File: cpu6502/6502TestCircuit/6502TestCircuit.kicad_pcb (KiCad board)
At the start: 4 copper layers, 45.7 x 40.6 mm, 15 parts, among them J1 Power, J2 Power, J5 Ext RST, SW1 Reset, U6 L7805, U9 DS1813

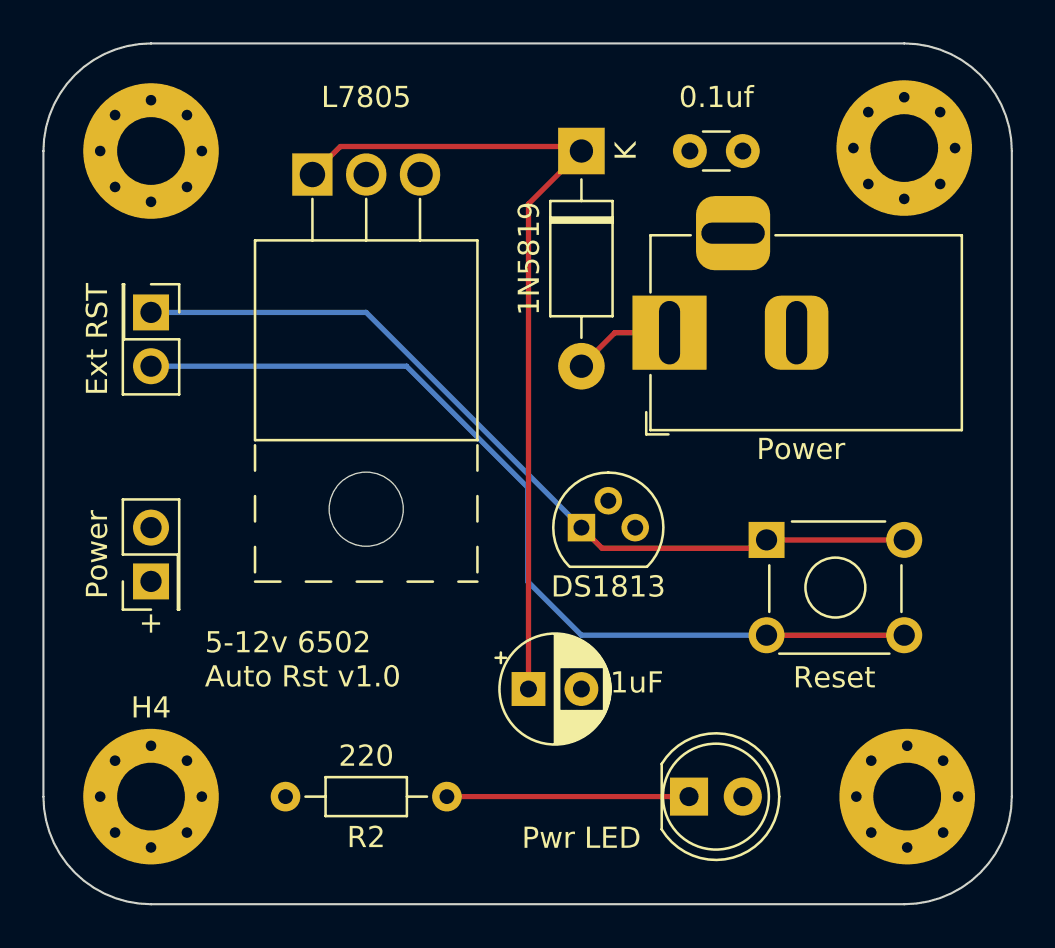
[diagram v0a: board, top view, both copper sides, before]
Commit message: Sent test circuit to PCBWay
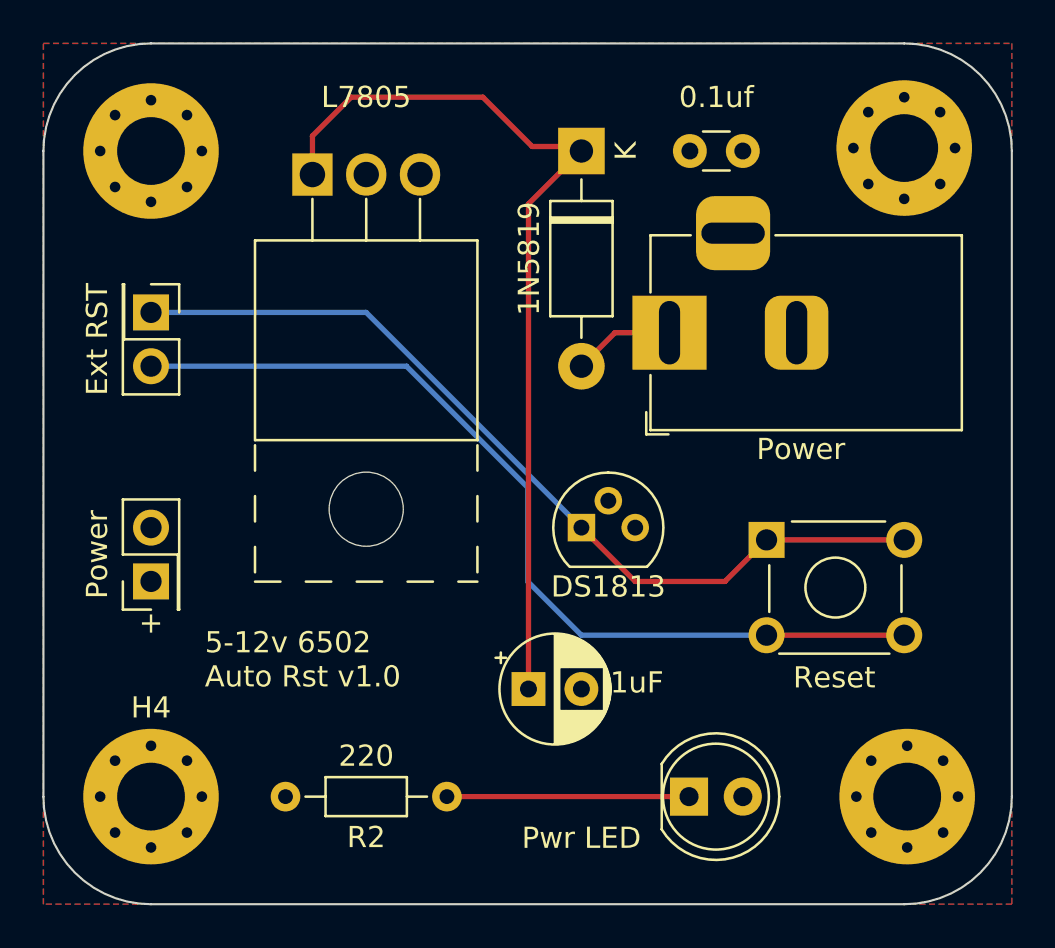
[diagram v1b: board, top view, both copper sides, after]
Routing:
- net Net-(D3-K): track 39.8 -> 42.8 mm
- net Net-(J5-Pin_1): track 40.3 -> 41.6 mm
- added copper zone on B.Cu, net +5V
- added copper zone on F.Cu, net GND
- removed copper zone on In2.Cu, net +5V
- removed copper zone on In1.Cu, net GND
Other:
- copper layers 4 -> 2
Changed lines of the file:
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@@
   (layers
     (0 "F.Cu" signal)
-    (1 "In1.Cu" power "GND")
-    (2 "In2.Cu" power "PWR")
     (31 "B.Cu" signal)
     (32 "B.Adhes" user "B.Adhesive")
@@
       (layer "F.Mask" (type "Top Solder Mask") (thickness 0.01))
       (layer "F.Cu" (type "copper") (thickness 0.035))
-      (layer "dielectric 1" (type "prepreg") (thickness 0.1) (material "FR4") (epsilon_r 4.5) (loss_tangent 0.02))
-      (layer "In1.Cu" (type "copper") (thickness 0.035))
-      (layer "dielectric 2" (type "core") (thickness 1.24) (material "FR4") (epsilon_r 4.5) (loss_tangent 0.02))
-      (layer "In2.Cu" (type "copper") (thickness 0.035))
-      (layer "dielectric 3" (type "prepreg") (thickness 0.1) (material "FR4") (epsilon_r 4.5) (loss_tangent 0.02))
+      (layer "dielectric 1" (type "core") (thickness 1.51) (material "FR4") (epsilon_r 4.5) (loss_tangent 0.02))
       (layer "B.Cu" (type "copper") (thickness 0.035))
       (layer "B.Mask" (type "Bottom Solder Mask") (thickness 0.01))
@@
     (effects (font (size 1 1) (thickness 0.15)) (justify bottom))
   )
-  (segment (start 142.025 73.445) (end 130.865 73.445) (width 0.25) (layer "F.Cu") (net 1))
+  (segment (start 137.59 71.12) (end 131.365 71.12) (width 0.25) (layer "F.Cu") (net 1))
+  (segment (start 129.54 72.945) (end 129.54 74.77) (width 0.25) (layer "F.Cu") (net 1))
+  (segment (start 131.365 71.12) (end 129.54 72.945) (width 0.25) (layer "F.Cu") (net 1))
   (segment (start 139.74 76.16) (end 142.24 73.66) (width 0.25) (layer "F.Cu") (net 1))
-  (segment (start 130.865 73.445) (end 129.54 74.77) (width 0.25) (layer "F.Cu") (net 1))
+  (segment (start 142.025 73.445) (end 139.915 73.445) (width 0.25) (layer "F.Cu") (net 1))
+  (segment (start 139.915 73.445) (end 137.59 71.12) (width 0.25) (layer "F.Cu") (net 1))
+  (segment (start 139.74 99.06) (end 139.74 76.16) (width 0.25) (layer "F.Cu") (net 1))
   (segment (start 142.24 73.66) (end 142.025 73.445) (width 0.25) (layer "F.Cu") (net 1))
-  (segment (start 139.74 99.06) (end 139.74 76.16) (width 0.25) (layer "F.Cu") (net 1))
   (segment (start 135.89 104.14) (end 147.32 104.14) (width 0.25) (layer "F.Cu") (net 4))
   (segment (start 143.8225 82.2375) (end 142.24 83.82) (width 0.25) (layer "F.Cu") (net 5))
   (segment (start 146.4 82.2375) (end 143.8225 82.2375) (width 0.25) (layer "F.Cu") (net 5))
-  (segment (start 143.215 92.415) (end 142.24 91.44) (width 0.25) (layer "F.Cu") (net 6))
+  (segment (start 149.02 93.98) (end 144.78 93.98) (width 0.25) (layer "F.Cu") (net 6))
   (segment (start 157.48 92.02) (end 150.98 92.02) (width 0.25) (layer "F.Cu") (net 6))
-  (segment (start 150.98 92.02) (end 150.585 92.415) (width 0.25) (layer "F.Cu") (net 6))
-  (segment (start 150.585 92.415) (end 143.215 92.415) (width 0.25) (layer "F.Cu") (net 6))
+  (segment (start 150.98 92.02) (end 149.02 93.98) (width 0.25) (layer "F.Cu") (net 6))
+  (segment (start 144.78 93.98) (end 142.24 91.44) (width 0.25) (layer "F.Cu") (net 6))
   (segment (start 121.92 81.28) (end 132.08 81.28) (width 0.25) (layer "B.Cu") (net 6))
   (segment (start 132.08 81.28) (end 142.24 91.44) (width 0.25) (layer "B.Cu") (net 6))
@@
   (segment (start 139.7 93.98) (end 142.24 96.52) (width 0.25) (layer "B.Cu") (net 7))
   (segment (start 142.24 96.52) (end 150.98 96.52) (width 0.25) (layer "B.Cu") (net 7))
-  (zone (net 2) (net_name "GND") (layer "In1.Cu") (hatch edge 0.5)
+  (zone (net 2) (net_name "GND") (layer "F.Cu") (hatch edge 0.5)
     (connect_pads (clearance 0.5))
     (min_thickness 0.25) (filled_areas_thickness no)
@@
     )
   )
-  (zone (net 3) (net_name "+5V") (layer "In2.Cu") (hatch edge 0.5)
+  (zone (net 3) (net_name "+5V") (layer "B.Cu") (hatch edge 0.5)
     (priority 1)
     (connect_pads (clearance 0.5))

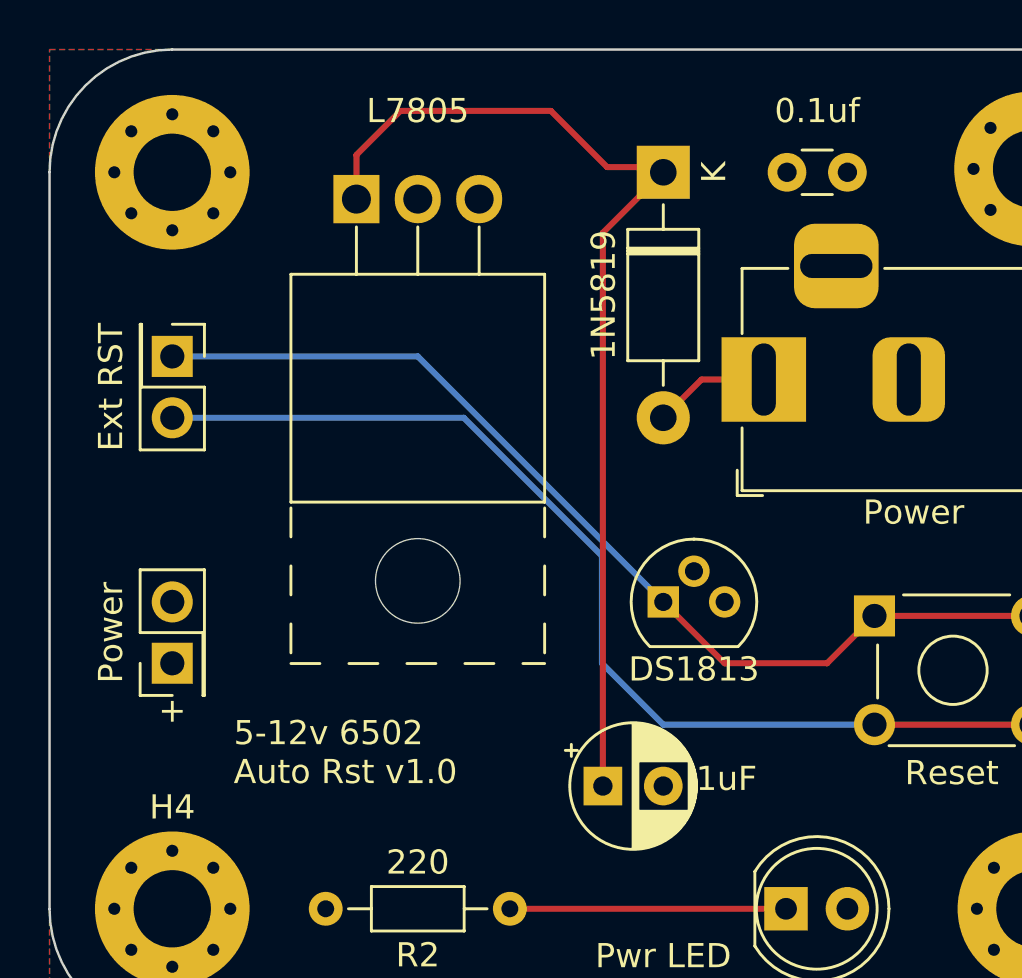
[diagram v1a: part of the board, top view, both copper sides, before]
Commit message: PCB: Add RS232 RCV LED, get pours connected, CODE: checkpoint
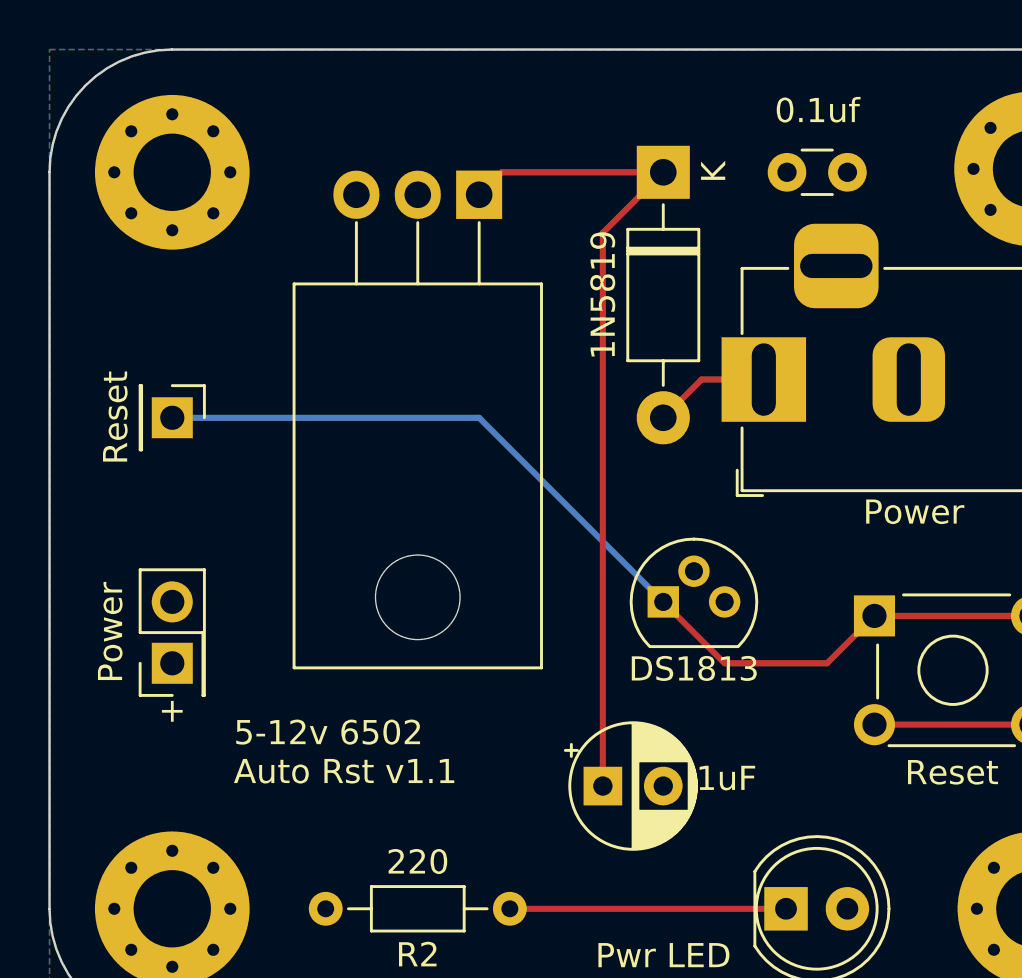
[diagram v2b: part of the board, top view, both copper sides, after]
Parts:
- removed J5: Ext RST, Connector_PinHeader_2.54mm:PinHeader_2x01_P2.54mm_Vertical
- added J3: Reset, Connector_PinHeader_2.54mm:PinHeader_1x01_P2.54mm_Vertical, F.Cu at (121.9, 83.8)
- C7: value 1uF -> 1uF
- U6: footprint Package_TO_SOT_THT:TO-220F-3_Horizontal_TabUp -> Package_TO_SOT_THT:TO-220-3_Horizontal_TabDown
- moved U6 5.08 mm to (134.6, 74.6), turned to 180 degrees
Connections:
- SW1 pad 1: Net-(J5-Pin_1) -> /RST
- SW1 pad 2: /RST -> GND
- U9 pad 1: Net-(J5-Pin_1) -> /RST
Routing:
- net Net-(J5-Pin_1): track 41.6 -> 0.00 mm
- net Net-(D3-K): track 42.8 -> 34.4 mm
- net GND: track 0.00 -> 6.50 mm
- net /RST: track 43.4 -> 40.6 mm
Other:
- board text added: "5-12v 6502 Auto Rst v1.1"
- board text removed: "5-12v 6502 Auto Rst v1.0"

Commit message: code changes (wip), set test PCB 2.0 to PCBway
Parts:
- removed C8: 0.1uf, Capacitor_THT:C_Disc_D3.0mm_W1.6mm_P2.50mm
- removed SW1: Reset, Button_Switch_THT:SW_TH_Tactile_Omron_B3F-10xx
- removed U6: L7805, Package_TO_SOT_THT:TO-220-3_Horizontal_TabDown
- added C1: 1uF, Capacitor_THT:CP_Radial_D5.0mm_P2.50mm, F.Cu at (106.7, 53.3)
- added C2: 0.1uf, Capacitor_THT:C_Disc_D3.0mm_W1.6mm_P2.50mm, F.Cu at (114.3, 71.1)
- added C3: 20pf, Capacitor_THT:C_Disc_D3.0mm_W1.6mm_P2.50mm, F.Cu at (100.3, 61.0)
- added C4: 1uf, Capacitor_THT:C_Disc_D3.0mm_W1.6mm_P2.50mm, F.Cu at (86.4, 38.1)
- added C5: 1uf, Capacitor_THT:C_Disc_D3.0mm_W1.6mm_P2.50mm, F.Cu at (100.3, 45.7)
- added C6: 1uf, Capacitor_THT:C_Disc_D3.0mm_W1.6mm_P2.50mm, F.Cu at (100.3, 48.3)
- added D2: Power LED, LED_THT:LED_D5.0mm, F.Cu at (110.5, 88.9)
- added D4: Rec, LED_THT:LED_D3.0mm, F.Cu at (114.3, 35.6)
- added J4: Power, Connector_BarrelJack:BarrelJack_Horizontal, F.Cu at (109.6, 63.2)
- added J5: RS232, TerminalBlock_TE-Connectivity:TerminalBlock_TE_282834-3_1x03_P2.54mm_Horizontal, F.Cu at (119.4, 43.2)
- added R3: 220, Resistor_THT:R_Axial_DIN0204_L3.6mm_D1.6mm_P7.62mm_Horizontal, F.Cu at (102.9, 86.4)
- added R4: 1M, Resistor_THT:R_Axial_DIN0204_L3.6mm_D1.6mm_P7.62mm_Horizontal, F.Cu at (92.7, 66.0)
- added R5: 220, Resistor_THT:R_Axial_DIN0207_L6.3mm_D2.5mm_P2.54mm_Vertical, F.Cu at (109.2, 36.8)
- added RV2: Contrast (10K), Potentiometer_THT:Potentiometer_Bourns_3386P_Vertical, F.Cu at (71.1, 81.3)
- added SW2: Debug, Button_Switch_THT:SW_TH_Tactile_Omron_B3F-10xx, F.Cu at (97.1, 27.0)
- added SW3: Reset, Button_Switch_THT:SW_TH_Tactile_Omron_B3F-10xx, F.Cu at (65.9, 88.2)
- added SW4: IRQ, Button_Switch_THT:SW_DIP_SPSTx03_Slide_6.7x9.18mm_W7.62mm_P2.54mm_LowProfile, F.Cu at (90.2, 94.0)
- added U1: 6522 (VIA), Package_DIP:DIP-40_W15.24mm_Socket, F.Cu at (43.2, 36.8)
- added U4: L7805, Package_TO_SOT_THT:TO-220-3_Horizontal_TabDown, F.Cu at (119.7, 81.3)
- added U5: DS1813, Package_TO_SOT_THT:TO-92, F.Cu at (96.5, 78.7)
- added U8: MAX232, Package_DIP:DIP-16_W7.62mm_Socket, F.Cu at (86.4, 43.2)
- added Y1: 1.8432 Mhz, Crystal:Crystal_HC49-4H_Vertical, F.Cu at (81.3, 81.3)
- C7: value 1uF -> 1uf; footprint Capacitor_THT:CP_Radial_D5.0mm_P2.50mm -> Capacitor_THT:C_Disc_D3.0mm_W1.6mm_P2.50mm
- D1: value Pwr LED -> 1N5819; footprint LED_THT:LED_D5.0mm -> Diode_THT:D_DO-41_SOD81_P10.16mm_Horizontal
- D3: value 1N5819 -> SB140
- J1: value Power -> CPU; footprint Connector_BarrelJack:BarrelJack_Horizontal -> Connector_PinHeader_2.54mm:PinHeader_1x19_P2.54mm_Vertical
- J2: value Power -> IRQ; footprint Connector_PinHeader_2.54mm:PinHeader_2x01_P2.54mm_Vertical -> Connector_PinHeader_2.54mm:PinHeader_1x01_P2.54mm_Vertical
- J3: value Reset -> LCD; footprint Connector_PinHeader_2.54mm:PinHeader_1x01_P2.54mm_Vertical -> Connector_PinHeader_2.54mm:PinHeader_1x16_P2.54mm_Vertical
- R2: value 220 -> 1K; footprint Resistor_THT:R_Axial_DIN0204_L3.6mm_D1.6mm_P7.62mm_Horizontal -> Resistor_THT:R_Axial_DIN0204_L3.6mm_D1.6mm_P2.54mm_Vertical
- U9: value DS1813 -> 6551 (ACIA); footprint Package_TO_SOT_THT:TO-92 -> Package_DIP:DIP-28_W15.24mm_Socket
- moved H3 145.0 mm to (34.3, 27.9)
- moved H2 124.5 mm to (34.3, 91.4)
- moved J1 117.8 mm to (41.9, 27.9), turned to 90 degrees
- moved J3 100.0 mm to (34.3, 35.6), turned to 0 degrees
- moved R2 78.3 mm to (109.2, 30.5), turned to 90 degrees
- moved H4 76.2 mm to (119.5, 27.9)
- moved U9 64.7 mm to (81.3, 69.9), turned to 180 degrees
- moved D1 63.4 mm to (94.0, 69.8)
- moved C7 60.4 mm to (100.3, 53.3), turned to -90 degrees
- moved D3 53.4 mm to (88.9, 72.4)
- moved J2 40.7 mm to (81.3, 92.7), turned to 0 degrees
- moved H1 17.9 mm to (119.5, 91.4)
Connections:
- C7 pad 1: Net-(D3-K) -> Net-(U8-C2+)
- C7 pad 2: GND -> Net-(U8-C2-)
- D1 pad 2: +5V -> Net-(D1-A)
- D3 pad 2: Net-(D3-A) -> /ACIAIRQ
- J1 pad 1: Net-(D3-A) -> /D0
- J1 pad 2: GND -> /D1
- J1 pad 3: (no net) -> /D2
- J2 pad 1: +5V -> /IRQ
- J3 pad 1: /RST -> GND
- R2 pad 1: Net-(D1-K) -> +5V
- R2 pad 2: GND -> /CA1
- U9 pad 1: /RST -> GND
- U9 pad 2: +5V -> /A12
- U9 pad 3: GND -> /CS2
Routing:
- net +5V: track 0.00 -> 309.6 mm
- net /RST: track 40.6 -> 141.5 mm, vias 0 -> 2
- net /D4: track 0.00 -> 76.9 mm
- net /CS2: track 0.00 -> 71.8 mm, vias 0 -> 2
- net /D3: track 0.00 -> 70.7 mm
- net Net-(J3-Pin_3): track 0.00 -> 65.0 mm, vias 0 -> 1
- net /D2: track 0.00 -> 64.7 mm
- net /R/W: track 0.00 -> 64.3 mm, vias 0 -> 1
- net /CA1: track 0.00 -> 60.5 mm
- net /PHI2: track 0.00 -> 59.5 mm, vias 0 -> 2
- net /A13: track 0.00 -> 58.9 mm, vias 0 -> 1
- net /A0: track 0.00 -> 58.5 mm
- net /D1: track 0.00 -> 58.3 mm
- net /D7: track 0.00 -> 56.8 mm
- net /D6: track 0.00 -> 56.2 mm
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- added copper zone on B.Cu, net GND
- removed copper zone on B.Cu, net +5V
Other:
- board size 45.7 x 40.6 mm -> 95.2 x 73.7 mm
- board text added: "6502 Test v2.0, Chris Gall"
- board text added: "A0"
- board text added: "A1"
- board text added: "A12"
- board text added: "A13"
- board text added: "A2"
- board text added: "A3"
- board text added: "ACIA"
- board text added: "CS2"
- board text added: "D0"
- board text added: "D1"
- board text added: "D2"
- board text added: "D3"
- board text added: "D4"
- board text added: "D5"
- board text added: "D6"
- board text added: "D7"
- board text added: "GND"
- board text added: "PHI2"
- board text added: "R/W"
- board text added: "RST"
- board text added: "Rx"
- board text added: "Tx"
- board text added: "VIA"
- board text added: "X"
- board text removed: "+"
- board text removed: "5-12v 6502 Auto Rst v1.1"

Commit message: checkpoint, most significantly OS works!!
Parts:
- J1: footprint Connector_PinHeader_2.54mm:PinHeader_1x19_P2.54mm_Vertical -> Connector_PinHeader_2.54mm:PinHeader_1x20_P2.54mm_Vertical
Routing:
- net +5V: track 309.6 -> 315.2 mm
- net /A1: track 55.3 -> 51.7 mm
- net /A0: track 58.5 -> 60.4 mm
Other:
- board text added: "6502 Test v2.1, Chris Gall"
- board text removed: "6502 Test v2.0, Chris Gall"
